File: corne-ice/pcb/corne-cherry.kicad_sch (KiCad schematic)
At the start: 92 parts, among them J1 MJ-4PP-9, J2 OLED, J3 MJ-4PP-9, J4 OLED, SW1 SW_PUSH, SW10 SW_PUSH, SW11 SW_PUSH, SW12 SW_PUSH, SW13 SW_PUSH, SW14 SW_PUSH, SW15 SW_PUSH, SW16 SW_PUSH, SW17 SW_PUSH, SW18 SW_PUSH, SW19 SW_PUSH, SW2 SW_PUSH, SW20 SW_PUSH, SW21 SW_PUSH, SW22 SW_PUSH, SW23 SW_PUSH, SW24 SW_PUSH, SW25 SW_PUSH, SW26 SW_PUSH, SW27 SW_PUSH, SW28 SW_PUSH, SW29 SW_PUSH, SW3 SW_PUSH, SW30 SW_PUSH, SW31 SW_PUSH, SW32 SW_PUSH, SW33 SW_PUSH, SW34 SW_PUSH, SW35 SW_PUSH, SW36 SW_PUSH, SW37 SW_PUSH, SW38 SW_PUSH, SW39 SW_PUSH, SW4 SW_PUSH, SW40 SW_PUSH, SW41 SW_PUSH, SW42 SW_PUSH, SW5 SW_PUSH, SW6 SW_PUSH, SW7 SW_PUSH, SW8 SW_PUSH, SW9 SW_PUSH, U1 ProMicro, U2 ProMicro

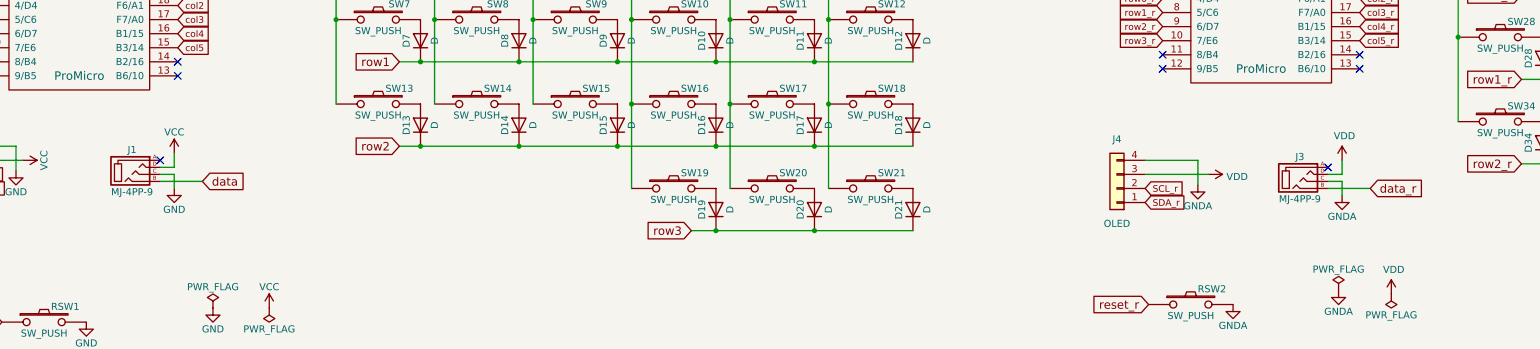
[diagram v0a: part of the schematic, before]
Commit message: remove trrs
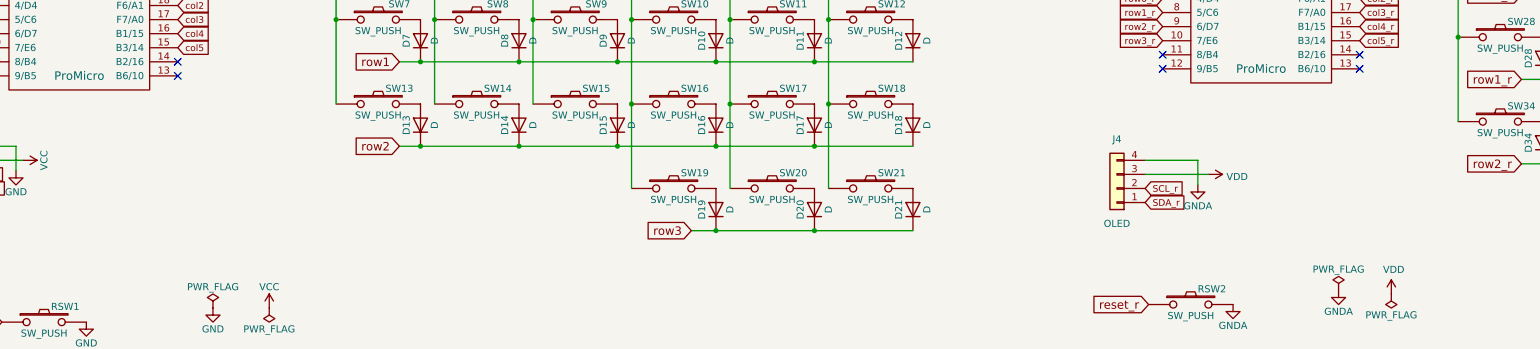
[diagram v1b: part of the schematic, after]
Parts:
- removed J1, J3: MJ-4PP-9, kbd:MJ-4PP-9_1side, symbol kbd:MJ-4PP-9
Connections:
- no-connect marks 12 -> 10
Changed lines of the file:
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@@
   (no_connect (at 62.865 55.245))
   (no_connect (at 240.665 53.975))
-  (no_connect (at 59.69 73.025))
   (no_connect (at 276.225 56.515))
   (no_connect (at 27.305 55.245))
   (no_connect (at 62.865 57.785))
-  (no_connect (at 270.51 74.295))
   (no_connect (at 276.225 53.975))
   (no_connect (at 240.665 56.515))
@@
     (stroke (width 0) (type default) (color 0 0 0 0))
   )
-  (wire (pts (xy 270.51 78.105) (xy 278.13 78.105))
-    (stroke (width 0) (type default) (color 0 0 0 0))
-  )
   (wire (pts (xy 142.24 55.245) (xy 160.02 55.245))
     (stroke (width 0) (type default) (color 0 0 0 0))
@@
     (stroke (width 0) (type default) (color 0 0 0 0))
   )
-  (wire (pts (xy 62.23 74.295) (xy 62.23 71.755))
-    (stroke (width 0) (type default) (color 0 0 0 0))
-  )
   (wire (pts (xy 160.02 40.005) (xy 177.8 40.005))
     (stroke (width 0) (type default) (color 0 0 0 0))
@@
     (stroke (width 0) (type default) (color 0 0 0 0))
   )
-  (wire (pts (xy 59.69 74.295) (xy 62.23 74.295))
-    (stroke (width 0) (type default) (color 0 0 0 0))
-  )
   (wire (pts (xy 237.49 73.025) (xy 247.015 73.025))
     (stroke (width 0) (type default) (color 0 0 0 0))
@@
     (stroke (width 0) (type default) (color 0 0 0 0))
   )
-  (wire (pts (xy 59.69 75.565) (xy 62.23 75.565))
-    (stroke (width 0) (type default) (color 0 0 0 0))
-  )
-  (wire (pts (xy 273.05 75.565) (xy 273.05 73.025))
-    (stroke (width 0) (type default) (color 0 0 0 0))
-  )
   (wire (pts (xy 365.125 66.04) (xy 365.125 81.28))
     (stroke (width 0) (type default) (color 0 0 0 0))
@@
     (stroke (width 0) (type default) (color 0 0 0 0))
   )
-  (wire (pts (xy 270.51 75.565) (xy 273.05 75.565))
-    (stroke (width 0) (type default) (color 0 0 0 0))
-  )
   (wire (pts (xy 329.565 31.75) (xy 329.565 35.56))
     (stroke (width 0) (type default) (color 0 0 0 0))
@@
     (stroke (width 0) (type default) (color 0 0 0 0))
   )
-  (wire (pts (xy 273.05 76.835) (xy 273.05 79.375))
-    (stroke (width 0) (type default) (color 0 0 0 0))
-  )
   (wire (pts (xy 305.435 73.66) (xy 309.245 73.66))
     (stroke (width 0) (type default) (color 0 0 0 0))
@@
     (stroke (width 0) (type default) (color 0 0 0 0))
   )
-  (wire (pts (xy 62.23 75.565) (xy 62.23 78.105))
-    (stroke (width 0) (type default) (color 0 0 0 0))
-  )
   (wire (pts (xy 91.44 28.575) (xy 91.44 32.385))
     (stroke (width 0) (type default) (color 0 0 0 0))
@@
     (stroke (width 0) (type default) (color 0 0 0 0))
   )
-  (wire (pts (xy 59.69 76.835) (xy 67.31 76.835))
-    (stroke (width 0) (type default) (color 0 0 0 0))
-  )
   (wire (pts (xy 62.865 32.385) (xy 67.945 32.385))
     (stroke (width 0) (type default) (color 0 0 0 0))
@@
   )
   (wire (pts (xy 33.655 74.93) (xy 33.655 70.485))
-    (stroke (width 0) (type default) (color 0 0 0 0))
-  )
-  (wire (pts (xy 270.51 76.835) (xy 273.05 76.835))
     (stroke (width 0) (type default) (color 0 0 0 0))
   )
@@
     )
   )
-  (global_label "data" (shape input) (at 67.31 76.835 0) (fields_autoplaced)
-    (effects (font (size 1.524 1.524)) (justify left))
-    (property "Intersheet References" "${INTERSHEET_REFS}" (id 0) (at 0 0 0)
-      (effects (font (size 1.27 1.27)) hide)
-    )
-  )
   (global_label "LED_r" (shape input) (at 240.665 28.575 180) (fields_autoplaced)
     (effects (font (size 1.1938 1.1938)) (justify right))
@@
   (global_label "col0_r" (shape input) (at 276.225 38.735 0) (fields_autoplaced)
     (effects (font (size 1.1938 1.1938)) (justify left))
-    (property "Intersheet References" "${INTERSHEET_REFS}" (id 0) (at 0 0 0)
-      (effects (font (size 1.27 1.27)) hide)
-    )
-  )
-  (global_label "data_r" (shape input) (at 278.13 78.105 0) (fields_autoplaced)
-    (effects (font (size 1.524 1.524)) (justify left))
     (property "Intersheet References" "${INTERSHEET_REFS}" (id 0) (at 0 0 0)
       (effects (font (size 1.27 1.27)) hide)
@@
     (pin "1")
   )
-  (symbol (lib_id "power:VCC") (at 62.23 71.755 0) (unit 1)
-    (in_bom yes) (on_board yes)
-    (property "Reference" "#PWR010" (id 0) (at 62.23 75.565 0)
-      (effects (font (size 1.27 1.27)) hide)
-    )
-    (property "Value" "VCC" (id 1) (at 62.23 67.945 0))
-    (property "Footprint" "" (id 2) (at 62.23 71.755 0)
-      (effects (font (size 1.27 1.27)) hide)
-    )
-    (property "Datasheet" "" (id 3) (at 62.23 71.755 0)
-      (effects (font (size 1.27 1.27)) hide)
-    )
-    (pin "1")
-  )
-  (symbol (lib_id "power:GND") (at 62.23 78.105 0) (unit 1)
-    (in_bom yes) (on_board yes)
-    (property "Reference" "#PWR011" (id 0) (at 62.23 84.455 0)
-      (effects (font (size 1.27 1.27)) hide)
-    )
-    (property "Value" "GND" (id 1) (at 62.23 81.915 0))
-    (property "Footprint" "" (id 2) (at 62.23 78.105 0)
-      (effects (font (size 1.27 1.27)) hide)
-    )
-    (property "Datasheet" "" (id 3) (at 62.23 78.105 0)
-      (effects (font (size 1.27 1.27)) hide)
-    )
-    (pin "1")
-  )
   (symbol (lib_id "Connector_Generic:Conn_01x04") (at 20.955 75.565 180) (unit 1)
     (in_bom yes) (on_board yes)
@@
     )
     (pin "1")
-  )
-  (symbol (lib_id "kbd:MJ-4PP-9") (at 54.61 74.93 0) (unit 1)
-    (in_bom yes) (on_board yes)
-    (property "Reference" "J1" (id 0) (at 54.61 71.12 0))
-    (property "Value" "MJ-4PP-9" (id 1) (at 54.61 78.74 0))
-    (property "Footprint" "kbd:MJ-4PP-9_1side" (id 2) (at 61.595 70.485 0)
-      (effects (font (size 1.27 1.27)) hide)
-    )
-    (property "Datasheet" "" (id 3) (at 61.595 70.485 0)
-      (effects (font (size 1.27 1.27)) hide)
-    )
-    (pin "A")
-    (pin "B")
-    (pin "C")
-    (pin "D")
   )
   (symbol (lib_id "kbd:ProMicro") (at 258.445 42.545 0) (unit 1)
@@
     (pin "1")
   )
-  (symbol (lib_id "power:GNDA") (at 273.05 79.375 0) (unit 1)
-    (in_bom yes) (on_board yes)
-    (property "Reference" "#PWR022" (id 0) (at 273.05 85.725 0)
-      (effects (font (size 1.27 1.27)) hide)
-    )
-    (property "Value" "GNDA" (id 1) (at 273.05 83.185 0))
-    (property "Footprint" "" (id 2) (at 273.05 79.375 0)
-      (effects (font (size 1.27 1.27)) hide)
-    )
-    (property "Datasheet" "" (id 3) (at 273.05 79.375 0)
-      (effects (font (size 1.27 1.27)) hide)
-    )
-    (pin "1")
-  )
   (symbol (lib_id "Connector_Generic:Conn_01x04") (at 232.41 78.105 180) (unit 1)
     (in_bom yes) (on_board yes)
@@
     (pin "1")
   )
-  (symbol (lib_id "kbd:MJ-4PP-9") (at 265.43 76.2 0) (unit 1)
-    (in_bom yes) (on_board yes)
-    (property "Reference" "J3" (id 0) (at 265.43 72.39 0))
-    (property "Value" "MJ-4PP-9" (id 1) (at 265.43 80.01 0))
-    (property "Footprint" "kbd:MJ-4PP-9_1side" (id 2) (at 272.415 71.755 0)
-      (effects (font (size 1.27 1.27)) hide)
-    )
-    (property "Datasheet" "" (id 3) (at 272.415 71.755 0)
-      (effects (font (size 1.27 1.27)) hide)
-    )
-    (pin "A")
-    (pin "B")
-    (pin "C")
-    (pin "D")
-  )
   (symbol (lib_id "power:VDD") (at 281.305 36.195 270) (unit 1)
     (in_bom yes) (on_board yes)
@@
     )
     (property "Datasheet" "" (id 3) (at 248.92 75.565 0)
-      (effects (font (size 1.27 1.27)) hide)
-    )
-    (pin "1")
-  )
-  (symbol (lib_id "power:VDD") (at 273.05 73.025 0) (unit 1)
-    (in_bom yes) (on_board yes)
-    (property "Reference" "#PWR021" (id 0) (at 273.05 76.835 0)
-      (effects (font (size 1.27 1.27)) hide)
-    )
-    (property "Value" "VDD" (id 1) (at 273.4818 68.6308 0))
-    (property "Footprint" "" (id 2) (at 273.05 73.025 0)
-      (effects (font (size 1.27 1.27)) hide)
-    )
-    (property "Datasheet" "" (id 3) (at 273.05 73.025 0)
       (effects (font (size 1.27 1.27)) hide)
     )
@@
       (reference "#PWR09") (unit 1) (value "VCC") (footprint "")
     )
-    (path "/00000000-0000-0000-0000-00005a76093e"
-      (reference "#PWR010") (unit 1) (value "VCC") (footprint "")
-    )
-    (path "/00000000-0000-0000-0000-00005a760adb"
-      (reference "#PWR011") (unit 1) (value "GND") (footprint "")
-    )
     (path "/00000000-0000-0000-0000-00005a923dd7"
       (reference "#PWR012") (unit 1) (value "VCC") (footprint "")
@@
       (reference "#PWR020") (unit 1) (value "GNDA") (footprint "")
     )
-    (path "/00000000-0000-0000-0000-00005c72b5f9"
-      (reference "#PWR021") (unit 1) (value "VDD") (footprint "")
-    )
-    (path "/00000000-0000-0000-0000-00005c25f992"
-      (reference "#PWR022") (unit 1) (value "GNDA") (footprint "")
-    )
     (path "/00000000-0000-0000-0000-00005c71de62"
       (reference "#PWR023") (unit 1) (value "VDD") (footprint "")
@@
       (reference "D42") (unit 1) (value "D") (footprint "kbd:D3_SMD_v2")
     )
-    (path "/00000000-0000-0000-0000-00005acd605d"
-      (reference "J1") (unit 1) (value "MJ-4PP-9") (footprint "kbd:MJ-4PP-9_1side")
-    )
     (path "/00000000-0000-0000-0000-00005a91da4b"
       (reference "J2") (unit 1) (value "OLED") (footprint "kbd:OLED_1side")
     )
-    (path "/00000000-0000-0000-0000-00005c25fa15"
-      (reference "J3") (unit 1) (value "MJ-4PP-9") (footprint "kbd:MJ-4PP-9_1side")
-    )
     (path "/00000000-0000-0000-0000-00005c25f9a2"
